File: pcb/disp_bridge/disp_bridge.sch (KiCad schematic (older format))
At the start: 5 parts, among them J1 CONN_01X21, J2 CONN_01X21, J3 CONN_01X21, J4 CONN_02X13, J5 CONN_02X13

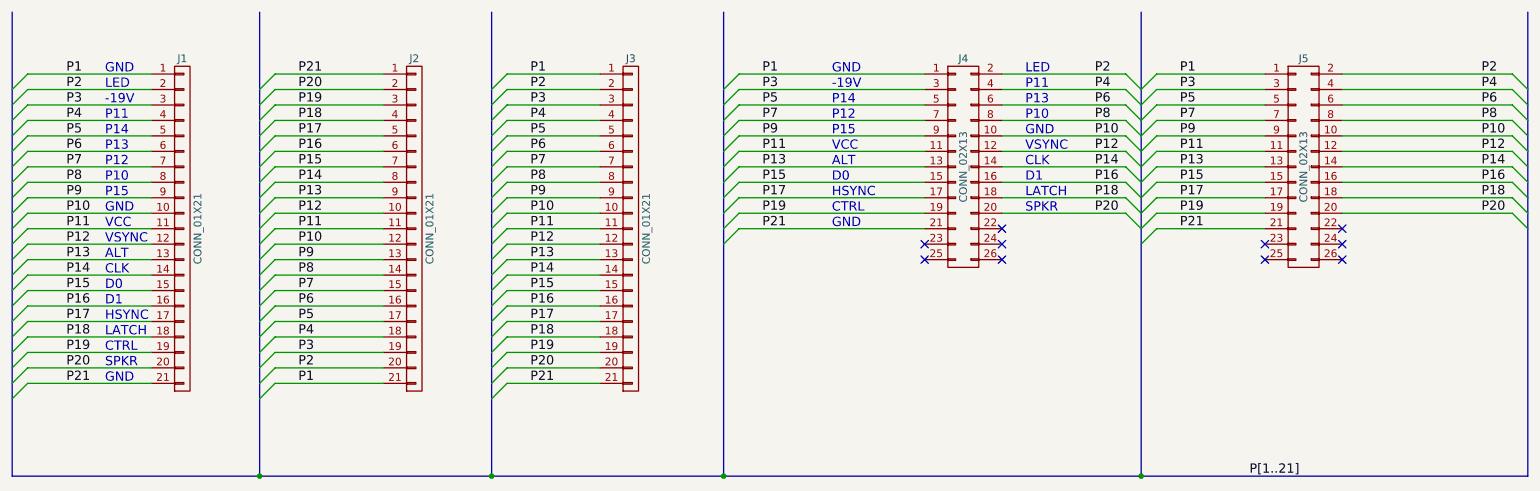
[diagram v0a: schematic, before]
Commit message: fix labeling of D0&D1 LCD signals
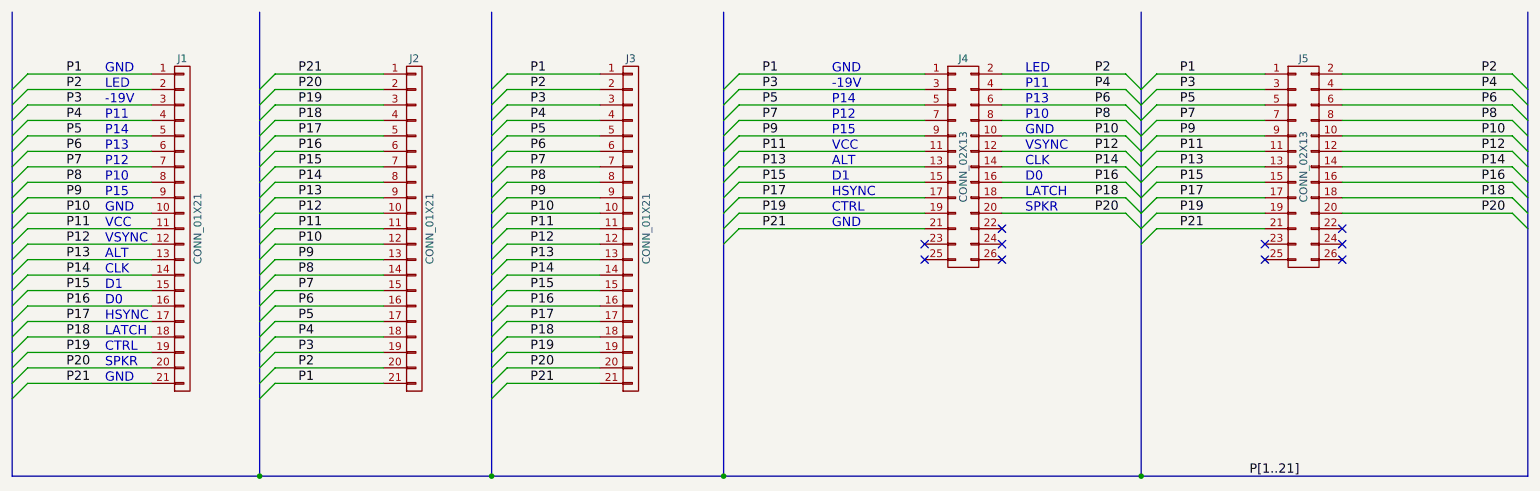
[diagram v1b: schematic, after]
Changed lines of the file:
@@
 Sheet 1 1
 Title "Display Bridge"
-Date "2019-08-10"
-Rev "0"
+Date "2019-10-06"
+Rev "1"
 Comp "Author: Michael Singer"
 Comment1 "https://sourceforge.net/projects/iceboy/"
@@
 CLK
 Text Notes 1300 4000 0    60   ~ 0
+D1
+Text Notes 1300 4100 0    60   ~ 0
 D0
-Text Notes 1300 4100 0    60   ~ 0
-D1
 Text Notes 1300 4200 0    60   ~ 0
 HSYNC
@@
 CLK
 Text Notes 6000 3300 0    60   ~ 0
+D1
+Text Notes 7250 3300 0    60   ~ 0
 D0
-Text Notes 7250 3300 0    60   ~ 0
-D1
 Text Notes 6000 3400 0    60   ~ 0
 HSYNC
